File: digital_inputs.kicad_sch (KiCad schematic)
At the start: 41 parts, among them J1 MMCX, J10 MMCX, J11 MMCX, J12 MMCX, J13 MMCX, J14 MMCX, J15 MMCX, J16 MMCX, J2 MMCX, J3 MMCX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

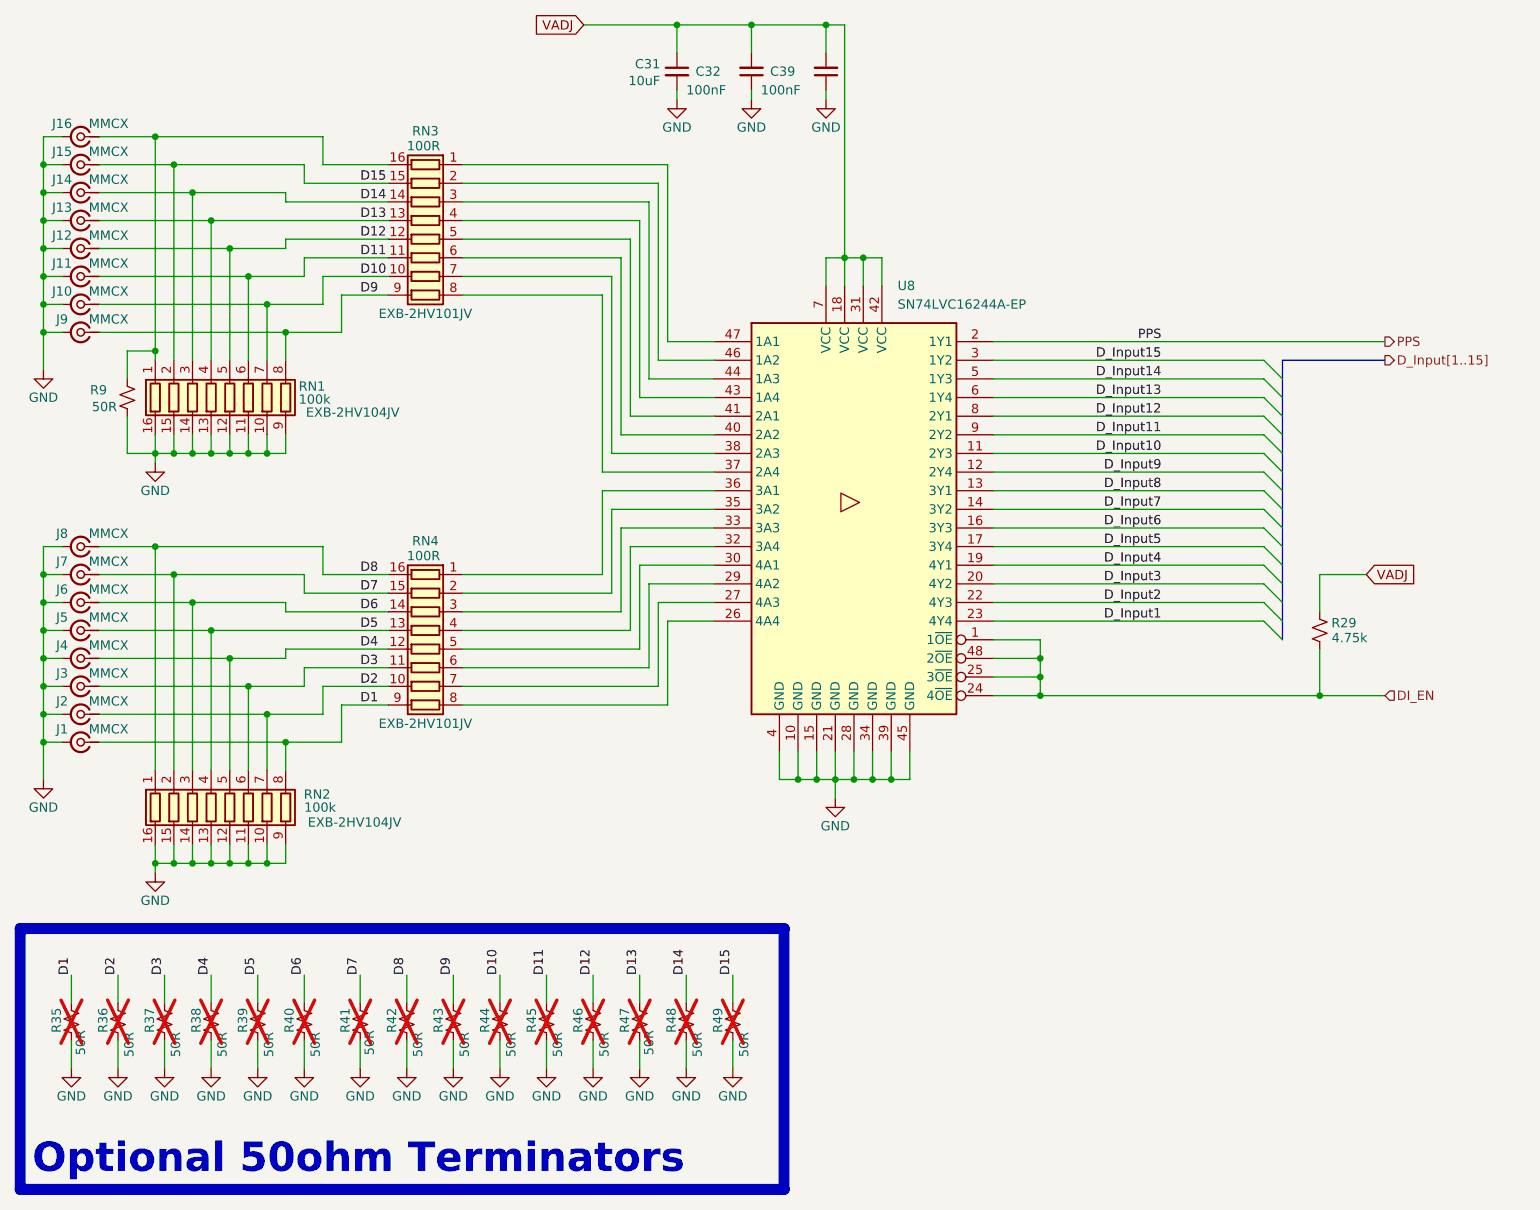
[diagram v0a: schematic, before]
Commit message: Updates before production run
- Changed mechanical mounting holes to slots for universal marble & FMC spec compatibility
- Moved Present trace coming from FMC pin H2 away from hole
- Moved Via near C29 a little away from the cap
- Moved optional 50 ohm terminations to be aligned between the connector row
- Shortened Traces leading to ADC inputs
- Changed thermal vias in ADC & CLK IC from 0.2mm -> 0.3mm holes
- Removed thermal relief spokes on ground layer connections of the thermal vias under IC's
- Enlarged Plane layer on "in2" layer for 'LMK_VCC_13" net for better connections
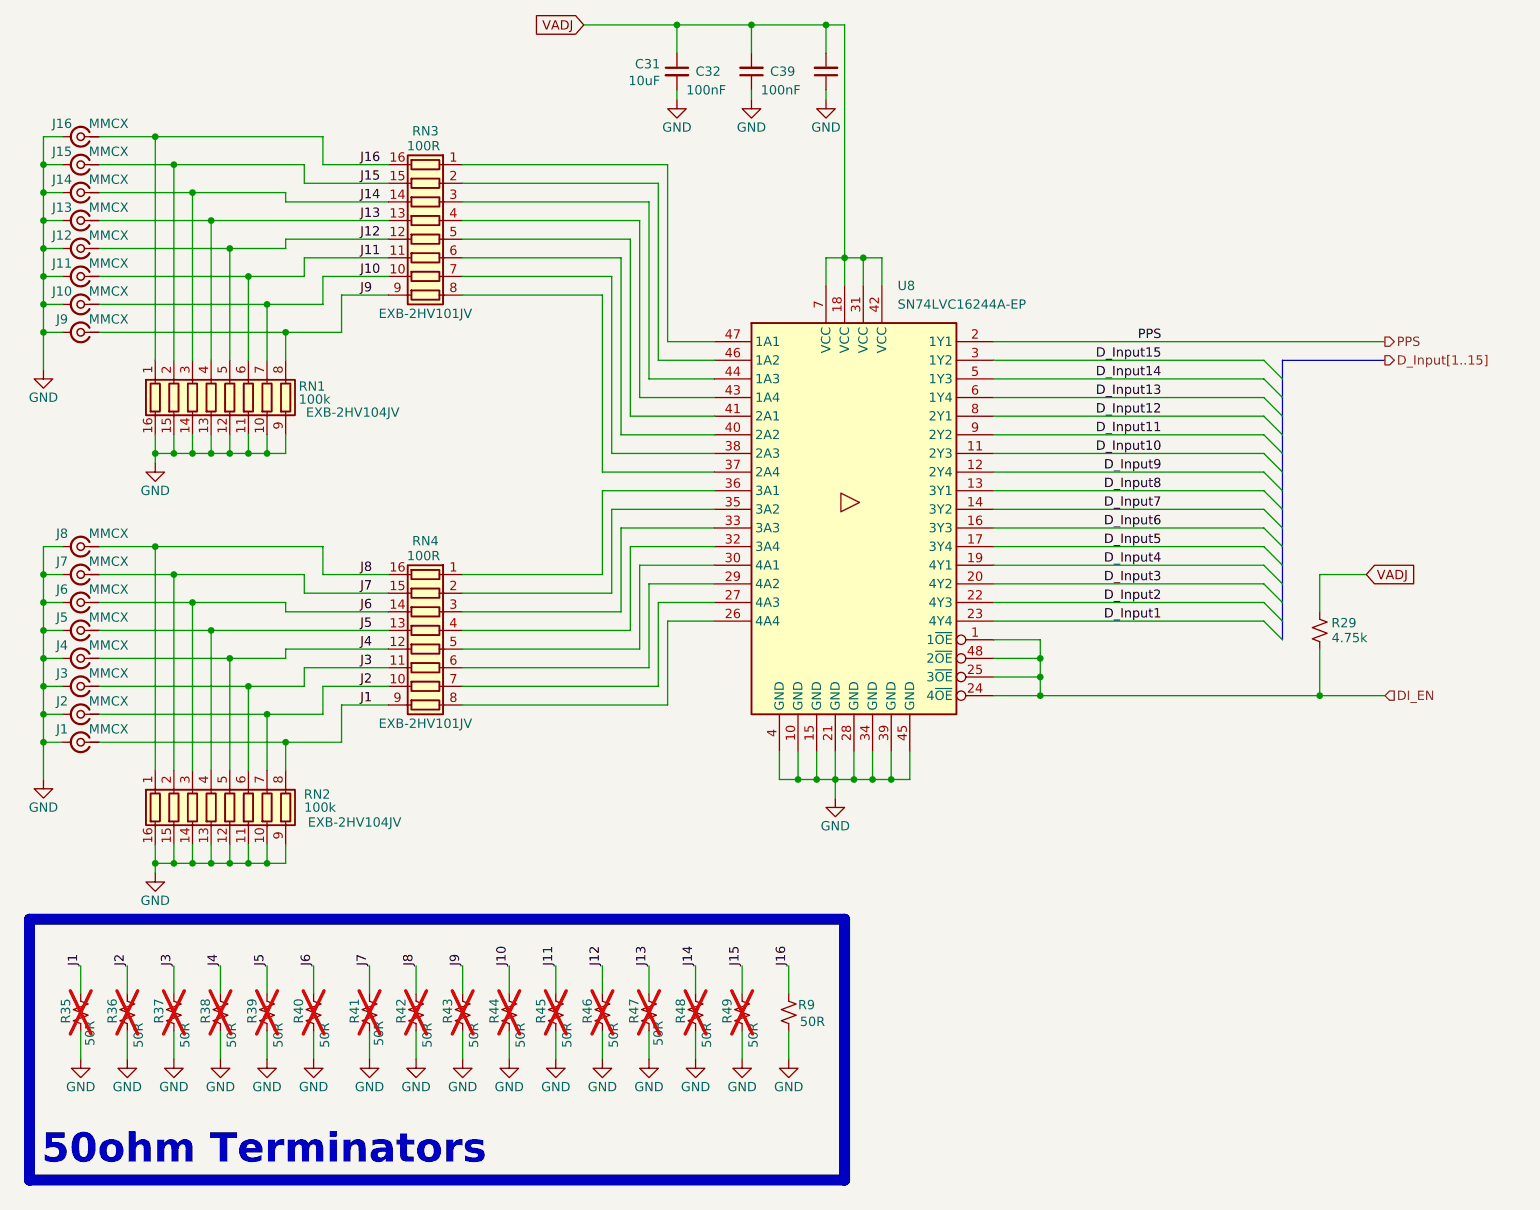
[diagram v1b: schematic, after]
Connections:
- net J16: now reaches J16.1 (In), R9.1, RN1.1 (R1.1), RN3.16 (R1.2)
- net D1 renamed J1
- net D10 renamed J10
- net D11 renamed J11
- net D12 renamed J12
- net D13 renamed J13
- net D14 renamed J14
- net D15 renamed J15
- net D2 renamed J2
- net D3 renamed J3
- net D4 renamed J4
- net D5 renamed J5
- net D6 renamed J6
- net D7 renamed J7
- net D8 renamed J8
- net D9 renamed J9
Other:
- note added: "50ohm Terminators"
- note removed: "Optional 50ohm Terminators"
- moved on the sheet: R35, R36, R37, R38, R39, R40, R41, R42, R43, R44, R45, R46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

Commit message: Changed Title Blocks to Version 1.0
- changed title blocks
- changed silkscreen to add version number
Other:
- title: RF Input FMC Board -> Clock Input FMC Board
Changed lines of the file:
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@@
 	(paper "USLetter")
 	(title_block
-		(title "RF Input FMC Board")
-		(date "2025-10-16")
-		(rev "0.2")
+		(title "Clock Input FMC Board")
+		(date "2026-05-20")
+		(rev "1.0")
 		(company "SPDX-FileCopyrightText: 2025 Osprey DCS")
 		(comment 1 "SPDX-License-Identifier: CERN-OHL-S-2.0+")
